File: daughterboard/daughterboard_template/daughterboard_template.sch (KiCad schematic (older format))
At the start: 1 part

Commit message: started with daughterboard template layout
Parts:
- J1: renamed from J?; footprint SAMTEC_PCIE-064-02-X-D-RA -> hive:PCIexpress_x4_daughterboard
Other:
- note added: "You can implement 4 targets per daugtherboard.\nPlease use the corresponding hierarchical schematics for that.\n"
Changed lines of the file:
@@
 $EndDescr
 $Comp
-L hive:PCIE-064-Daughterboard J?
+L hive:PCIE-064-Daughterboard J1
 U 1 1 61657129
 P 5900 3150
-F 0 "J?" H 5900 5017 50  0000 C CNN
+F 0 "J1" H 5900 5017 50  0000 C CNN
 F 1 "PCIE-064-Daughterboard" H 5900 4926 50  0000 C CNN
-F 2 "SAMTEC_PCIE-064-02-X-D-RA" H 6100 3150 50  0001 L BNN
+F 2 "hive:PCIexpress_x4_daughterboard" H 6100 3150 50  0001 L BNN
 F 3 "" H 5900 3150 50  0001 L BNN
 F 4 "Samtec Inc" H 6100 3150 50  0001 L BNN "MANUFACTURER"
@@
 	6600 2050 7300 2050
 $Comp
-L power:PWR_FLAG #FLG?
+L power:PWR_FLAG #FLG0101
 U 1 1 6165E545
 P 4500 1550
-F 0 "#FLG?" H 4500 1625 50  0001 C CNN
+F 0 "#FLG0101" H 4500 1625 50  0001 C CNN
 F 1 "PWR_FLAG" V 4500 1850 50  0000 C CNN
 F 2 "" H 4500 1550 50  0001 C CNN
@@
 $EndComp
 $Comp
-L power:PWR_FLAG #FLG?
+L power:PWR_FLAG #FLG0102
 U 1 1 6165F06C
 P 7350 1750
-F 0 "#FLG?" H 7350 1825 50  0001 C CNN
+F 0 "#FLG0102" H 7350 1825 50  0001 C CNN
 F 1 "PWR_FLAG" V 7350 2050 50  0000 C CNN
 F 2 "" H 7350 1750 50  0001 C CNN
@@
 $EndComp
 $Comp
-L power:GND #PWR?
+L power:GND #PWR0101
 U 1 1 616603AB
 P 7300 1600
-F 0 "#PWR?" H 7300 1350 50  0001 C CNN
+F 0 "#PWR0101" H 7300 1350 50  0001 C CNN
 F 1 "GND" V 7305 1472 50  0000 R CNN
 F 2 "" H 7300 1600 50  0001 C CNN
@@
 $EndComp
 $Comp
-L power:GND #PWR?
+L power:GND #PWR0102
 U 1 1 616608FA
 P 7300 2050
-F 0 "#PWR?" H 7300 1800 50  0001 C CNN
+F 0 "#PWR0102" H 7300 1800 50  0001 C CNN
 F 1 "GND" V 7305 1922 50  0000 R CNN
 F 2 "" H 7300 2050 50  0001 C CNN
@@
 $EndComp
 $Comp
-L power:GND #PWR?
+L power:GND #PWR0103
 U 1 1 61660B9A
 P 4500 1800
-F 0 "#PWR?" H 4500 1550 50  0001 C CNN
+F 0 "#PWR0103" H 4500 1550 50  0001 C CNN
 F 1 "GND" V 4505 1672 50  0000 R CNN
 F 2 "" H 4500 1800 50  0001 C CNN
@@
 $EndComp
 $Comp
-L power:GND #PWR?
+L power:GND #PWR0104
 U 1 1 616612C5
 P 4500 2050
-F 0 "#PWR?" H 4500 1800 50  0001 C CNN
+F 0 "#PWR0104" H 4500 1800 50  0001 C CNN
 F 1 "GND" V 4505 1922 50  0000 R CNN
 F 2 "" H 4500 2050 50  0001 C CNN
@@
 $EndComp
 $Comp
-L power:+3V3 #PWR?
+L power:+3V3 #PWR0105
 U 1 1 6166171D
 P 7350 1850
-F 0 "#PWR?" H 7350 1700 50  0001 C CNN
+F 0 "#PWR0105" H 7350 1700 50  0001 C CNN
 F 1 "+3V3" V 7365 1978 50  0000 L CNN
 F 2 "" H 7350 1850 50  0001 C CNN
@@
 	4600 1550 4600 1650
 $Comp
-L power:+5V #PWR?
+L power:+5V #PWR0106
 U 1 1 616632B1
 P 4500 1650
-F 0 "#PWR?" H 4500 1500 50  0001 C CNN
+F 0 "#PWR0106" H 4500 1500 50  0001 C CNN
 F 1 "+5V" V 4515 1778 50  0000 L CNN
 F 2 "" H 4500 1650 50  0001 C CNN
@@
 	6600 2750 7300 2750
 $Comp
-L power:GND #PWR?
+L power:GND #PWR0107
 U 1 1 61664445
 P 7300 2750
-F 0 "#PWR?" H 7300 2500 50  0001 C CNN
+F 0 "#PWR0107" H 7300 2500 50  0001 C CNN
 F 1 "GND" V 7305 2622 50  0000 R CNN
 F 2 "" H 7300 2750 50  0001 C CNN
@@
 	6600 3350 7300 3350
 $Comp
-L power:GND #PWR?
+L power:GND #PWR0108
 U 1 1 6166496B
 P 7300 3350
-F 0 "#PWR?" H 7300 3100 50  0001 C CNN
+F 0 "#PWR0108" H 7300 3100 50  0001 C CNN
 F 1 "GND" V 7305 3222 50  0000 R CNN
 F 2 "" H 7300 3350 50  0001 C CNN
@@
 	6600 4050 7300 4050
 $Comp
-L power:GND #PWR?
+L power:GND #PWR0109
 U 1 1 61664EDA
 P 7300 4050
-F 0 "#PWR?" H 7300 3800 50  0001 C CNN
+F 0 "#PWR0109" H 7300 3800 50  0001 C CNN
 F 1 "GND" V 7305 3922 50  0000 R CNN
 F 2 "" H 7300 4050 50  0001 C CNN
@@
 	6600 4650 7300 4650
 $Comp
-L power:GND #PWR?
+L power:GND #PWR0110
 U 1 1 61665461
 P 7300 4650
-F 0 "#PWR?" H 7300 4400 50  0001 C CNN
+F 0 "#PWR0110" H 7300 4400 50  0001 C CNN
 F 1 "GND" V 7305 4522 50  0000 R CNN
 F 2 "" H 7300 4650 50  0001 C CNN
@@
 	5200 2650 4500 2650
 $Comp
-L power:GND #PWR?
+L power:GND #PWR0111
 U 1 1 61665D67
 P 4500 2650
-F 0 "#PWR?" H 4500 2400 50  0001 C CNN
+F 0 "#PWR0111" H 4500 2400 50  0001 C CNN
 F 1 "GND" V 4505 2522 50  0000 R CNN
 F 2 "" H 4500 2650 50  0001 C CNN
@@
 	5200 3350 4500 3350
 $Comp
-L power:GND #PWR?
+L power:GND #PWR0112
 U 1 1 6166639C
 P 4500 3350
-F 0 "#PWR?" H 4500 3100 50  0001 C CNN
+F 0 "#PWR0112" H 4500 3100 50  0001 C CNN
 F 1 "GND" V 4505 3222 50  0000 R CNN
 F 2 "" H 4500 3350 50  0001 C CNN
@@
 	5200 3950 4500 3950
 $Comp
-L power:GND #PWR?
+L power:GND #PWR0113
 U 1 1 61666A19
 P 4500 3950
-F 0 "#PWR?" H 4500 3700 50  0001 C CNN
+F 0 "#PWR0113" H 4500 3700 50  0001 C CNN
 F 1 "GND" V 4505 3822 50  0000 R CNN
 F 2 "" H 4500 3950 50  0001 C CNN
@@
 	5200 4650 4500 4650
 $Comp
-L power:GND #PWR?
+L power:GND #PWR0114
 U 1 1 61667143
 P 4500 4650
-F 0 "#PWR?" H 4500 4400 50  0001 C CNN
+F 0 "#PWR0114" H 4500 4400 50  0001 C CNN
 F 1 "GND" V 4505 4522 50  0000 R CNN
 F 2 "" H 4500 4650 50  0001 C CNN
@@
 $EndComp
 $Comp
-L power:+3V3 #PWR?
+L power:+3V3 #PWR0115
 U 1 1 61667838
 P 4500 1950
-F 0 "#PWR?" H 4500 1800 50  0001 C CNN
+F 0 "#PWR0115" H 4500 1800 50  0001 C CNN
 F 1 "+3V3" V 4515 2078 50  0000 L CNN
 F 2 "" H 4500 1950 50  0001 C CNN
@@
 Wire Wire Line
 	7950 4450 8800 4450
+Text Notes 750  800  0    50   ~ 0
+You can implement 4 targets per daugtherboard.\nPlease use the corresponding hierarchical schematics for that.\n
 $EndSCHEMATC

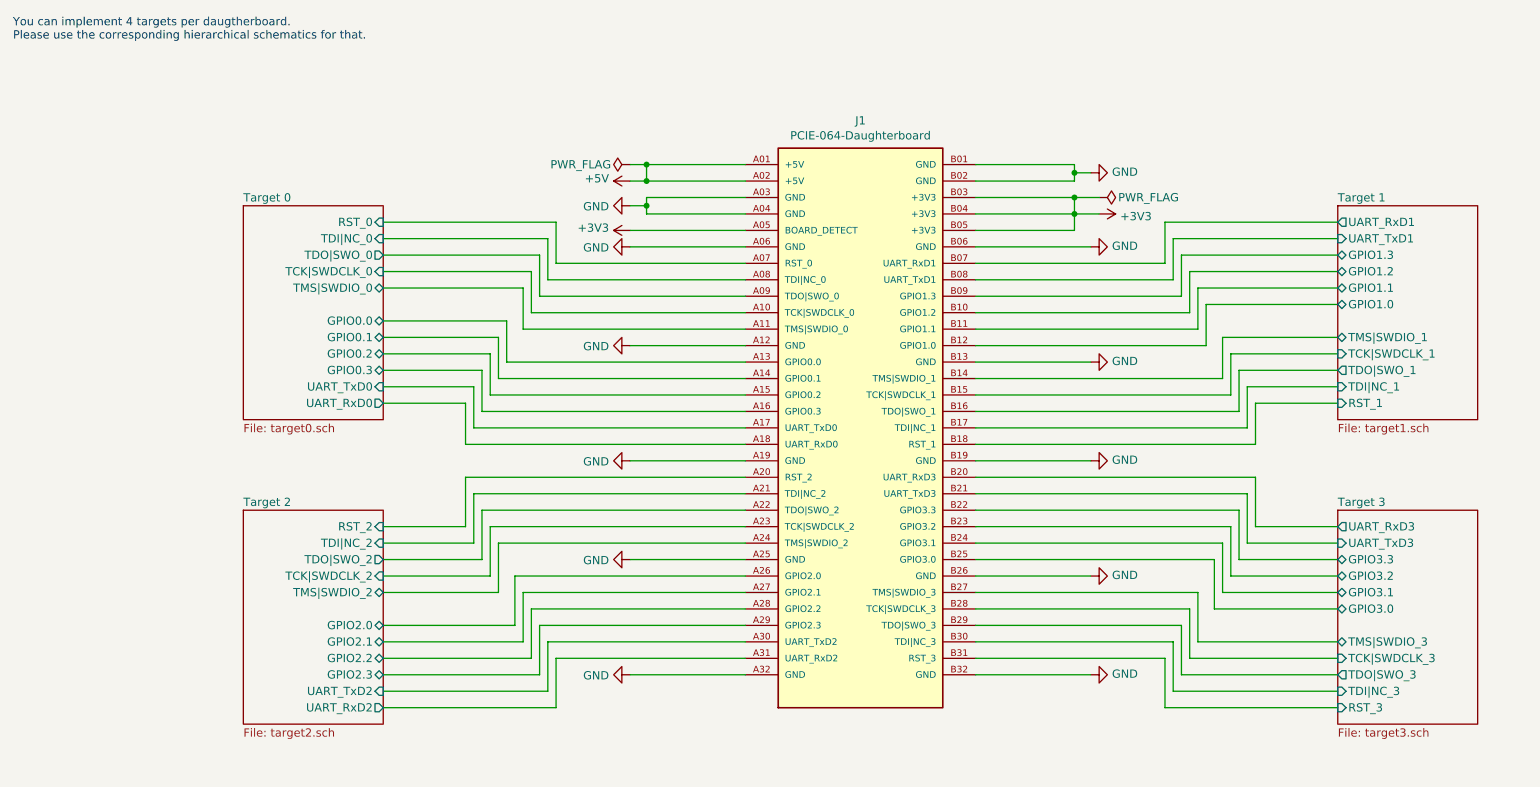
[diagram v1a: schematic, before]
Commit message: changed PCIE 64 to M.2 Key B connector
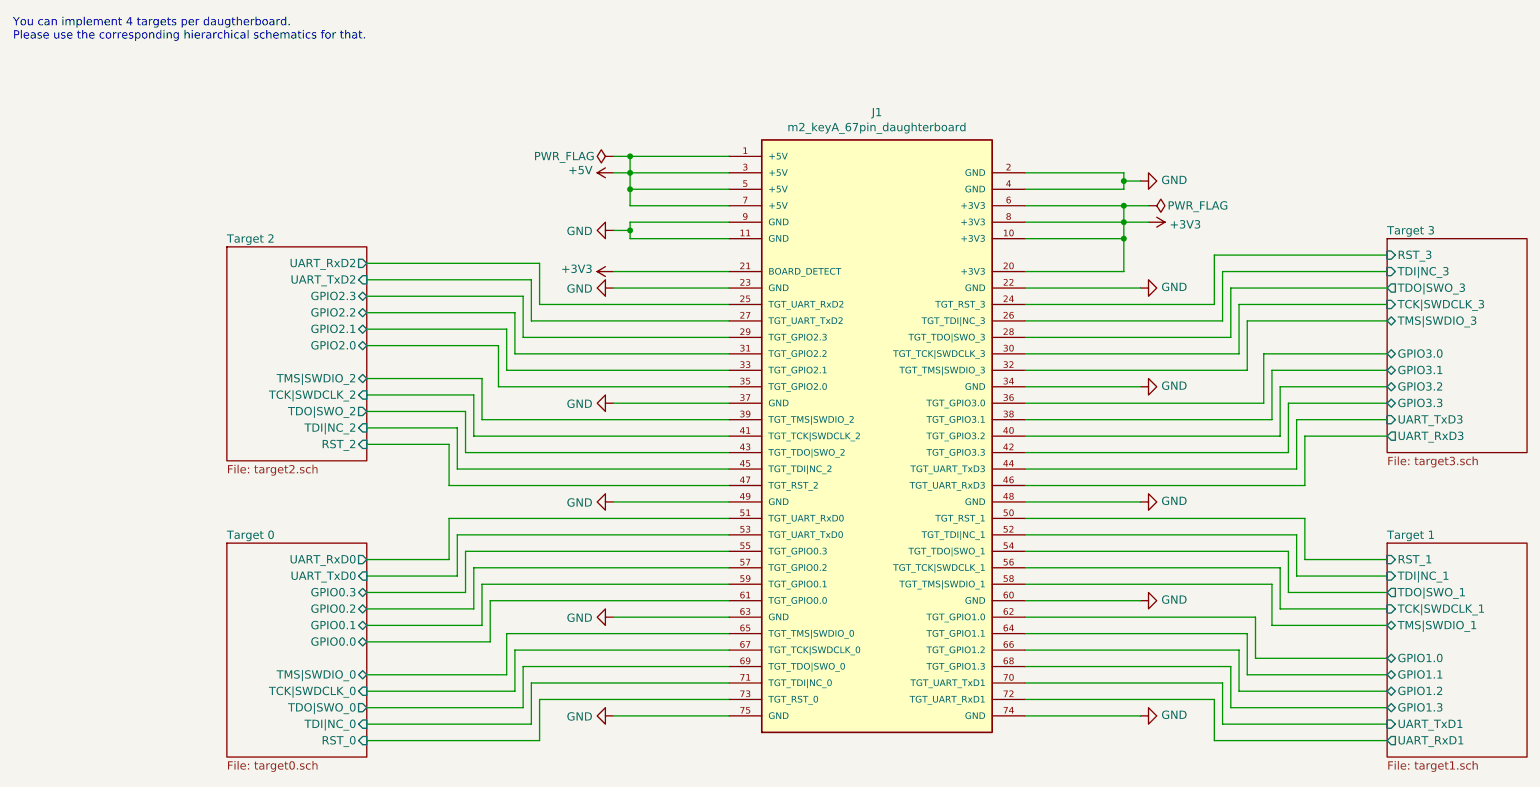
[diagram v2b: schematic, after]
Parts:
- removed J1: PCIE-064-Daughterboard, hive:PCIexpress_x4_daughterboard, symbol hive:PCIE-064-Daughterboard
- added J1: m2_keyA_67pin_daughterboard, hive:m2_keyB, symbol hive:m2_keyA_67pin_daughterboard
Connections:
- net +3V3: now also J1.10 (+3V3), J1.20 (+3V3), J1.21 (BOARD_DETECT), J1.6 (+3V3), J1.8 (+3V3)
- net +5V: now also J1.1 (+5V), J1.3 (+5V), J1.5 (+5V), J1.7 (+5V)
- net GND: now also J1.11 (GND), J1.2 (GND), J1.22 (GND), J1.23 (GND), J1.34 (GND), J1.37 (GND), J1.4 (GND), J1.48 (GND), J1.49 (GND), J1.60 (GND), J1.63 (GND), J1.74 (GND), J1.75 (GND), J1.9 (GND)
- net Target 0/GPIO0.0: now also J1.61 (TGT_GPIO0.0)
- net Target 0/GPIO0.1: now also J1.59 (TGT_GPIO0.1)
- net Target 0/GPIO0.2: now also J1.57 (TGT_GPIO0.2)
- net Target 0/GPIO0.3: now also J1.55 (TGT_GPIO0.3)
- net Target 0/RST_0: now also J1.73 (TGT_RST_0)
- net Target 0/TCK|SWDCLK_0: now also J1.67 (TGT_TCK|SWDCLK_0)
- net Target 0/TDI|NC_0: now also J1.71 (TGT_TDI|NC_0)
- net Target 0/TDO|SWO_0: now also J1.69 (TGT_TDO|SWO_0)
- net Target 0/TMS|SWDIO_0: now also J1.65 (TGT_TMS|SWDIO_0)
- net Target 0/UART_RxD0: now also J1.51 (TGT_UART_RxD0)
- net Target 0/UART_TxD0: now also J1.53 (TGT_UART_TxD0)
- net Target 1/GPIO1.0: now also J1.62 (TGT_GPIO1.0)
- net Target 1/GPIO1.1: now also J1.64 (TGT_GPIO1.1)
- net Target 1/GPIO1.2: now also J1.66 (TGT_GPIO1.2)
- net Target 1/GPIO1.3: now also J1.68 (TGT_GPIO1.3)
- net Target 1/RST_1: now also J1.50 (TGT_RST_1)
- net Target 1/TCK|SWDCLK_1: now also J1.56 (TGT_TCK|SWDCLK_1)
- net Target 1/TDI|NC_1: now also J1.52 (TGT_TDI|NC_1)
- net Target 1/TDO|SWO_1: now also J1.54 (TGT_TDO|SWO_1)
- net Target 1/TMS|SWDIO_1: now also J1.58 (TGT_TMS|SWDIO_1)
- net Target 1/UART_RxD1: now also J1.72 (TGT_UART_RxD1)
- net Target 1/UART_TxD1: now also J1.70 (TGT_UART_TxD1)
- net Target 2/GPIO2.0: now also J1.35 (TGT_GPIO2.0)
- net Target 2/GPIO2.1: now also J1.33 (TGT_GPIO2.1)
- net Target 2/GPIO2.2: now also J1.31 (TGT_GPIO2.2)
- net Target 2/GPIO2.3: now also J1.29 (TGT_GPIO2.3)
- net Target 2/RST_2: now also J1.47 (TGT_RST_2)
- net Target 2/TCK|SWDCLK_2: now also J1.41 (TGT_TCK|SWDCLK_2)
- net Target 2/TDI|NC_2: now also J1.45 (TGT_TDI|NC_2)
- net Target 2/TDO|SWO_2: now also J1.43 (TGT_TDO|SWO_2)
- net Target 2/TMS|SWDIO_2: now also J1.39 (TGT_TMS|SWDIO_2)
- net Target 2/UART_RxD2: now also J1.25 (TGT_UART_RxD2)
- net Target 2/UART_TxD2: now also J1.27 (TGT_UART_TxD2)
- net Target 3/GPIO3.0: now also J1.36 (TGT_GPIO3.0)
- net Target 3/GPIO3.1: now also J1.38 (TGT_GPIO3.1)
- net Target 3/GPIO3.2: now also J1.40 (TGT_GPIO3.2)
- net Target 3/GPIO3.3: now also J1.42 (TGT_GPIO3.3)
- net Target 3/RST_3: now also J1.24 (TGT_RST_3)
- net Target 3/TCK|SWDCLK_3: now also J1.30 (TGT_TCK|SWDCLK_3)
- net Target 3/TDI|NC_3: now also J1.26 (TGT_TDI|NC_3)
- net Target 3/TDO|SWO_3: now also J1.28 (TGT_TDO|SWO_3)
- net Target 3/TMS|SWDIO_3: now also J1.32 (TGT_TMS|SWDIO_3)
- net Target 3/UART_RxD3: now also J1.46 (TGT_UART_RxD3)
- net Target 3/UART_TxD3: now also J1.44 (TGT_UART_TxD3)

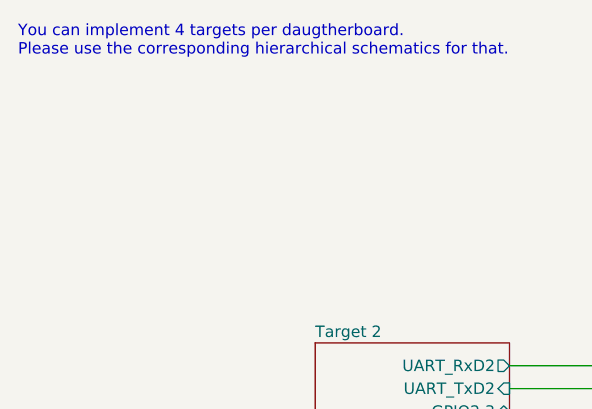
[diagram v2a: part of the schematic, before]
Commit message: added M2.5 Daughterboard backup mounting solution
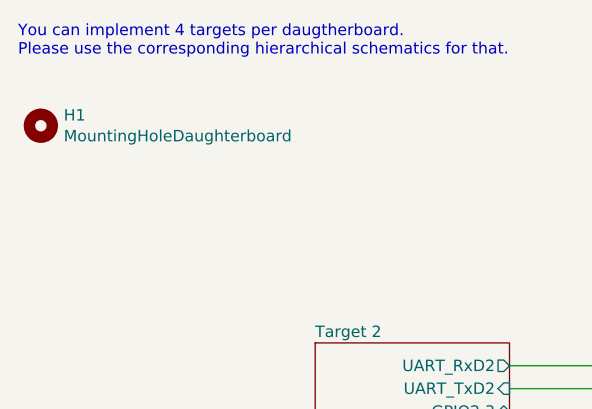
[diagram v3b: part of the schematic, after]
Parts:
- added H1: MountingHoleDaughterboard, MountingHole:MountingHole_2.7mm_M2.5, symbol Mechanical:MountingHole
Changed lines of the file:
@@
 Wire Wire Line
 	3400 3250 2900 3250
+$Comp
+L Mechanical:MountingHole H1
+U 1 1 61832037
+P 850 1100
+F 0 "H1" H 950 1146 50  0000 L CNN
+F 1 "MountingHoleDaughterboard" H 950 1055 50  0000 L CNN
+F 2 "MountingHole:MountingHole_2.7mm_M2.5" H 850 1100 50  0001 C CNN
+F 3 "~" H 850 1100 50  0001 C CNN
+	1    850  1100
+	1    0    0    -1
+$EndComp
 $EndSCHEMATC
